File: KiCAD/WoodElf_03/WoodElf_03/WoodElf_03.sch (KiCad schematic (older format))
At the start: 9 parts, among them T1 BlankThrough-Hole, T10 BlankThrough-Hole, T2 BlankThrough-Hole, T3 BlankThrough-Hole, T4 BlankThrough-Hole, T5 BlankThrough-Hole, T6 BlankThrough-Hole, T9 BlankThrough-Hole

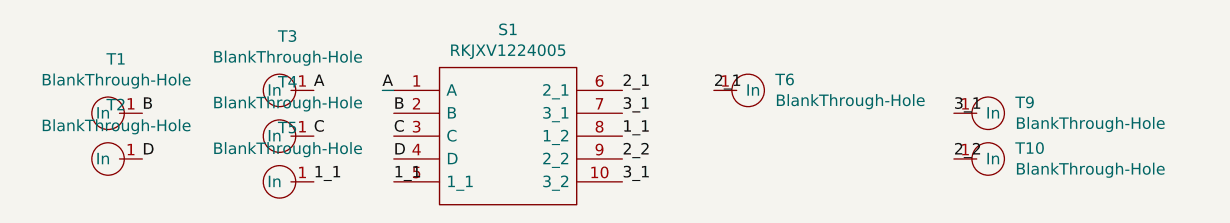
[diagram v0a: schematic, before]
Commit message: reworked the outer edge of the PCB
turns out i didnt consider how the tiling screw holes would fit with the wire holes - it should all be good now and not interfere with itself
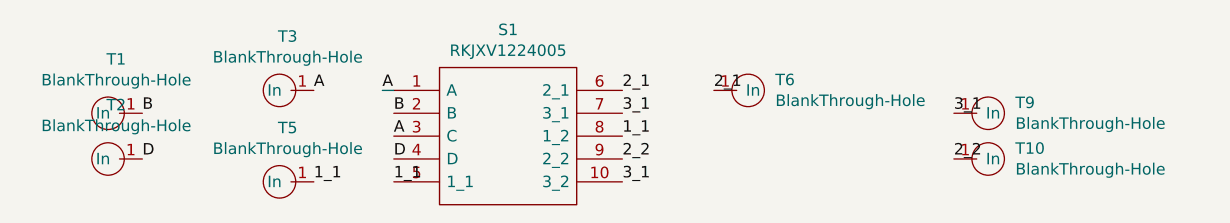
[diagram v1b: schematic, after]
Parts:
- removed T4: BlankThrough-Hole, WoodElf_Lib:BlankThrough-Hole, symbol WoodElf_01:BlankThrough-Hole
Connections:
- net C is gone; now on net A: S1.3 (C)
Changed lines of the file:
@@
-$EndComp
-$Comp
-L WoodElf_01:BlankThrough-Hole T4
-U 1 1 5CD58A34
-P 5050 3950
-F 0 "T4" H 5014 3714 50  0000 C CNN
-F 1 "BlankThrough-Hole" H 5014 3805 50  0000 C CNN
-F 2 "WoodElf_Lib:BlankThrough-Hole" H 5050 3950 50  0001 C CNN
-F 3 "" H 5050 3950 50  0001 C CNN
-	1    5050 3950
-	-1   0    0    1
 $EndComp
 $Comp
@@
 Text Label 4450 3850 0    50   ~ 0
 B
-Text Label 5200 3950 0    50   ~ 0
-C
 Text Label 5550 3950 0    50   ~ 0
-C
+A
 Text Label 5550 4050 0    50   ~ 0
 D
